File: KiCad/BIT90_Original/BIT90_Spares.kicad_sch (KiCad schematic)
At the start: 3 parts, among them U7 74LS74, U8 74LS05, U9 74LS32

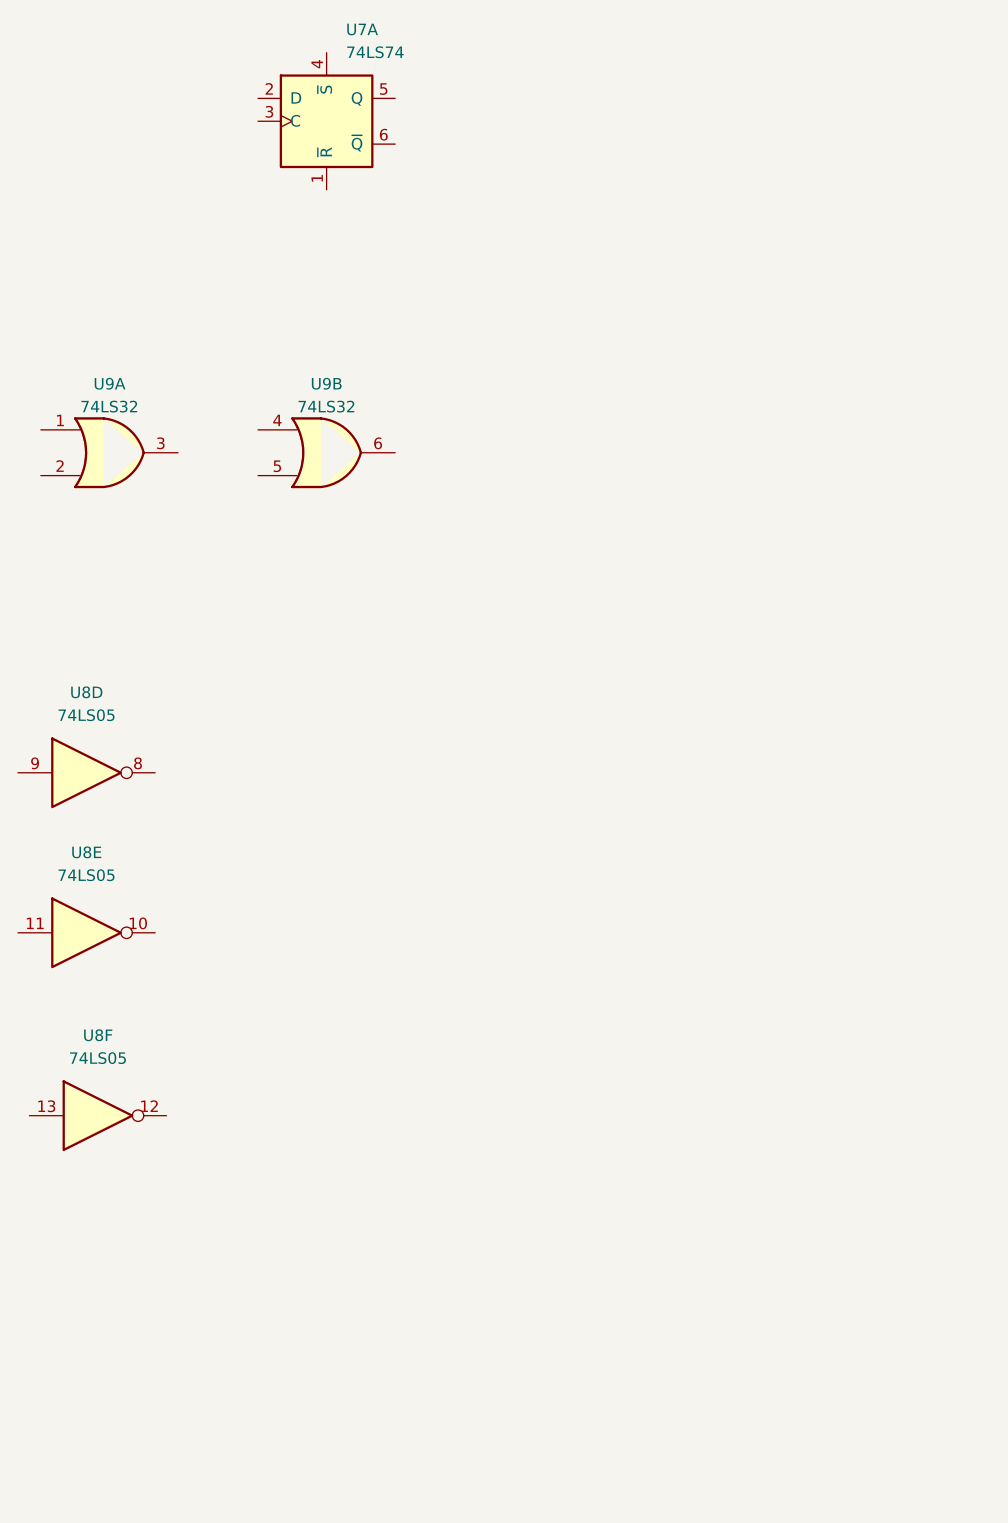
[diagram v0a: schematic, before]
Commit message: Added "Video Control" schematic
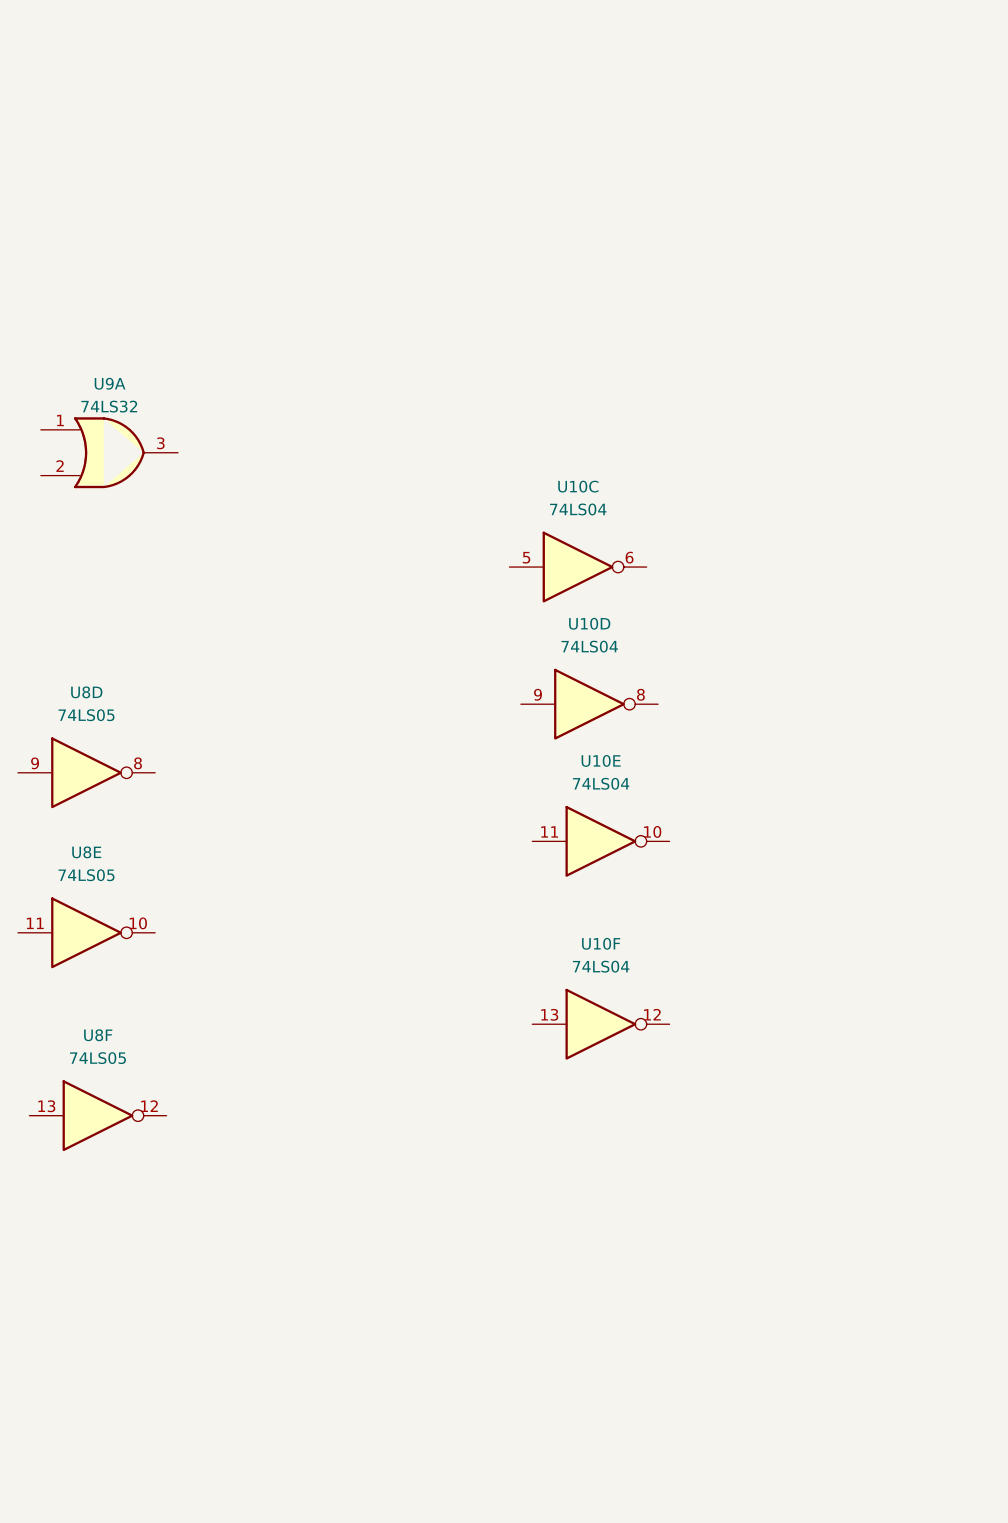
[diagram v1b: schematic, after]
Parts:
- removed U7: 74LS74, symbol 74xx:74LS74
- removed unit 2 of U9
- added U10: 74LS04, symbol 74xx:74LS04

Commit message: Added "Joystick, Audio, Tape Out" schematic
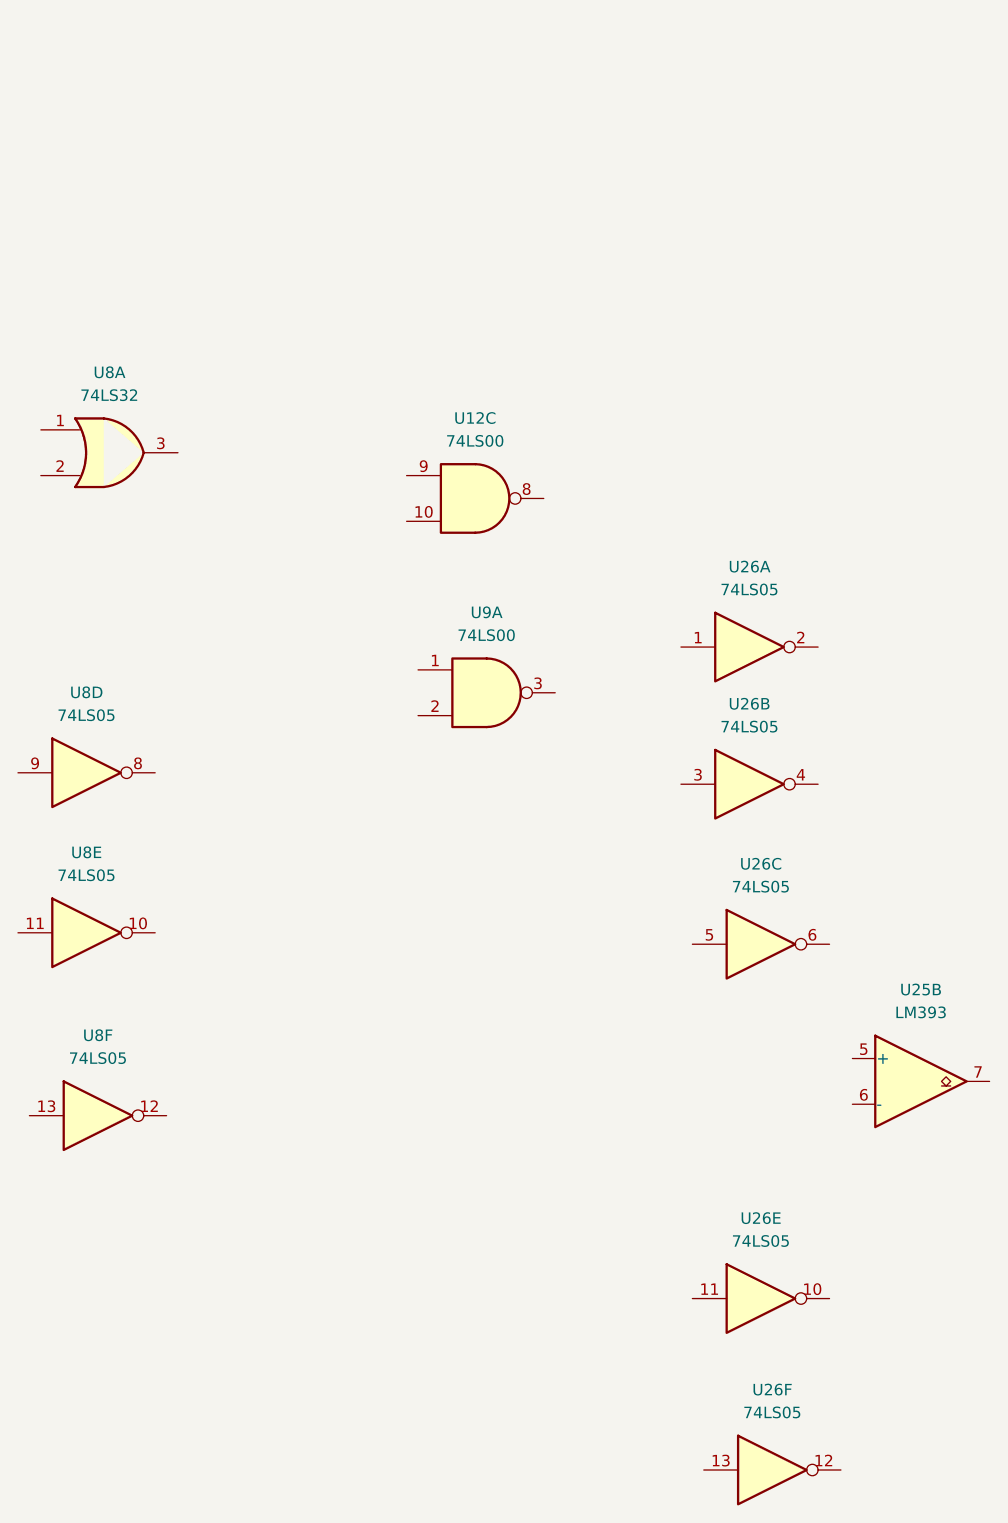
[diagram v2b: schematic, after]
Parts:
- removed U10: 74LS04, symbol 74xx:74LS04
- added U12, U9: 74LS00, symbol 74xx:74LS00
- added U25: LM393, symbol Comparator:LM393
- added U26: 74LS05, symbol 74xx:74LS05
- renumbered U9 to U8
